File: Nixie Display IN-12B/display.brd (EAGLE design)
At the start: 161.1 x 51.6 mm, 30 parts, among them U1 TPIC6B595DWRG4, U2 TPIC6B595DWRG4, U3 TPIC6B595DWRG4, U4 TPIC6B595DWRG4, U5 TPIC6B595DWRG4, U6 TPIC6B595DWRG4, U7 TPIC6B595DWRG4, U8 TPIC6B595DWRG4, X1 22-23-2021

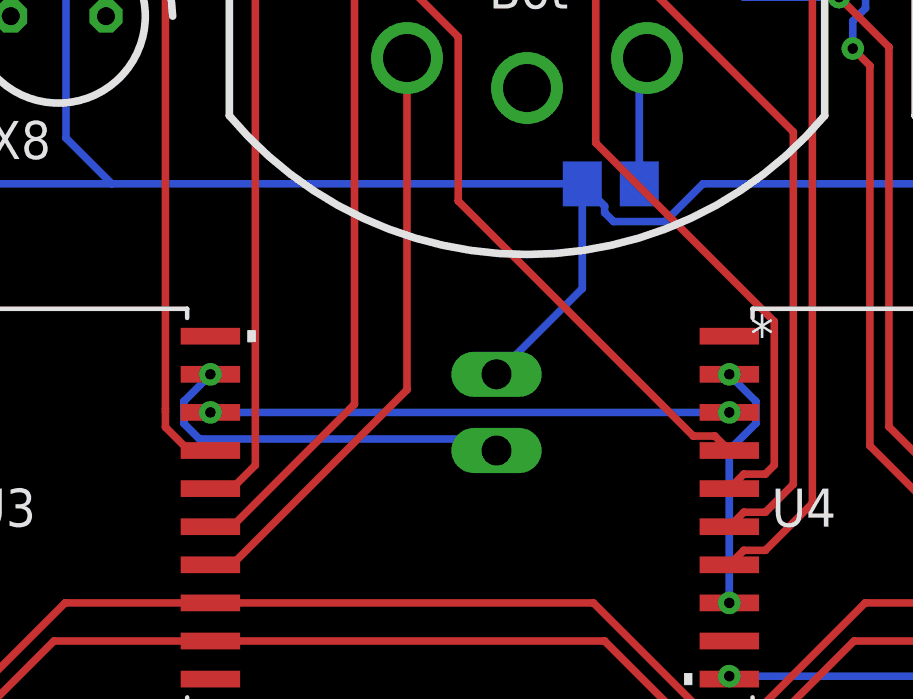
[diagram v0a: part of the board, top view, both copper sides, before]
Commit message: Begins sketch, fixes spacing and encoder circuit
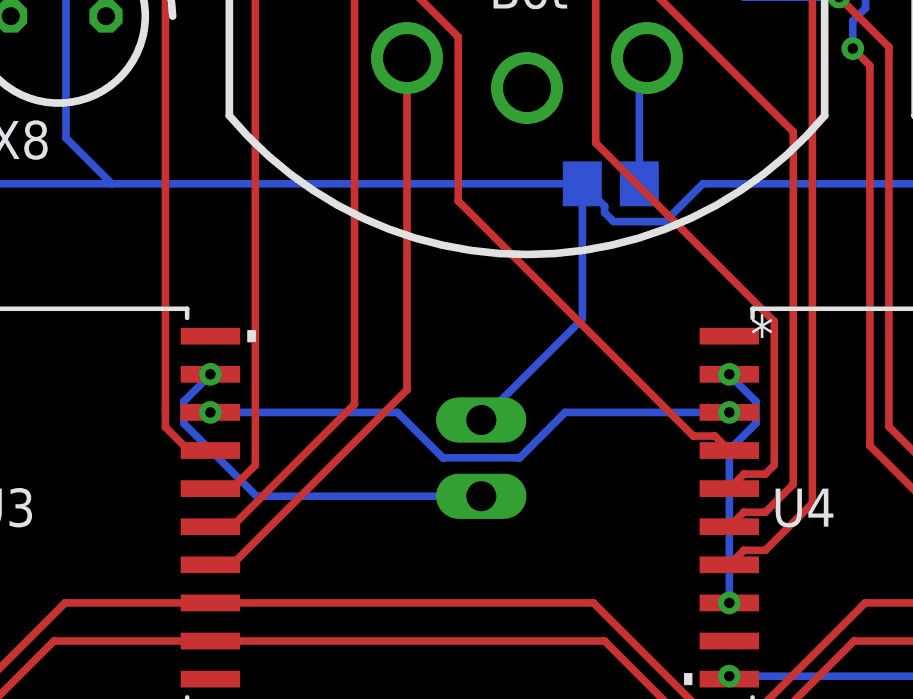
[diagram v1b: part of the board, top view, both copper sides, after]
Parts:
- moved X1 1.61 mm to (67.2, 15.1)
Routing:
- net V+: track 194.7 -> 196.5 mm
- net N$79: track 17.3 -> 18.6 mm
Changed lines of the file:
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@@
 <attribute name="VALUE" x="14.097" y="6.731" size="1.27" layer="27" ratio="10" rot="R180"/>
 </element>
-<element name="X1" library="con-molex" library_urn="urn:adsk.eagle:library:165" package="22-23-2021" package3d_urn="urn:adsk.eagle:package:8078633/1" value="22-23-2021" x="67.691" y="16.637" locked="yes" smashed="yes" rot="MR270">
-<attribute name="MF" value="MOLEX" x="67.691" y="16.637" locked="yes" size="1.778" layer="28" rot="MR270" display="off"/>
-<attribute name="MPN" value="22-23-2021" x="67.691" y="16.637" locked="yes" size="1.778" layer="28" rot="MR270" display="off"/>
-<attribute name="NAME" x="63.881" y="19.177" locked="yes" size="1.016" layer="26" ratio="10" rot="MR270"/>
-<attribute name="OC_FARNELL" value="1462926" x="67.691" y="16.637" locked="yes" size="1.778" layer="28" rot="MR270" display="off"/>
-<attribute name="OC_NEWARK" value="25C3832" x="67.691" y="16.637" locked="yes" size="1.778" layer="28" rot="MR270" display="off"/>
-<attribute name="POPULARITY" value="40" x="67.691" y="16.637" locked="yes" size="1.778" layer="28" rot="MR270" display="off"/>
-<attribute name="VALUE" x="72.771" y="19.177" locked="yes" size="1.016" layer="28" ratio="10" rot="MR270"/>
+<element name="X1" library="con-molex" library_urn="urn:adsk.eagle:library:165" package="22-23-2021" package3d_urn="urn:adsk.eagle:package:8078633/1" value="22-23-2021" x="67.183" y="15.113" smashed="yes" rot="MR270">
+<attribute name="MF" value="MOLEX" x="67.183" y="15.113" size="1.778" layer="28" rot="MR270" display="off"/>
+<attribute name="MPN" value="22-23-2021" x="67.183" y="15.113" size="1.778" layer="28" rot="MR270" display="off"/>
+<attribute name="NAME" x="63.373" y="17.653" size="1.016" layer="26" ratio="10" rot="MR270"/>
+<attribute name="OC_FARNELL" value="1462926" x="67.183" y="15.113" size="1.778" layer="28" rot="MR270" display="off"/>
+<attribute name="OC_NEWARK" value="25C3832" x="67.183" y="15.113" size="1.778" layer="28" rot="MR270" display="off"/>
+<attribute name="POPULARITY" value="40" x="67.183" y="15.113" size="1.778" layer="28" rot="MR270" display="off"/>
+<attribute name="VALUE" x="72.263" y="17.653" size="1.016" layer="28" ratio="10" rot="MR270"/>
 </element>
 <element name="NX1" library="nixies-us" package="IN-12-DSUB" value="" x="14.224" y="36.195" smashed="yes">
@@
 <via x="58.1533" y="17.907" extent="1-16" drill="0.35"/>
 <wire x1="57.2671" y1="17.00408125" x2="57.2671" y2="16.26991875" width="0.254" layer="16"/>
-<wire x1="57.2671" y1="16.26991875" x2="57.78621875" y2="15.7508" width="0.254" layer="16"/>
-<wire x1="67.3072" y1="15.7508" x2="67.691" y2="15.367" width="0.254" layer="16"/>
-<wire x1="57.78621875" y1="15.7508" x2="67.3072" y2="15.7508" width="0.254" layer="16"/>
 <wire x1="58.1533" y1="17.907" x2="58.1533" y2="17.89028125" width="0.254" layer="16"/>
 <wire x1="58.1533" y1="17.89028125" x2="57.2671" y2="17.00408125" width="0.254" layer="16"/>
@@
 <via x="147.0787" y="8.0998" extent="1-16" drill="0.35"/>
 <wire x1="147.0787" y1="8.0998" x2="147.0787" y2="8.001" width="0.254" layer="1"/>
+<wire x1="59.69401875" y1="13.843" x2="67.183" y2="13.843" width="0.254" layer="16"/>
+<wire x1="57.2671" y1="16.26991875" x2="59.69401875" y2="13.843" width="0.254" layer="16"/>
 </signal>
 <signal name="VCC">
@@
 <wire x1="51.496" y1="47.2936125" x2="52.5605" y2="46.2291125" width="0.254" layer="16"/>
 <wire x1="52.5605" y1="46.2291125" x2="52.5605" y2="42.7401" width="0.254" layer="16"/>
-<wire x1="70.551" y1="24.257" x2="70.551" y2="20.767" width="0.254" layer="16"/>
-<wire x1="70.551" y1="20.767" x2="67.691" y2="17.907" width="0.254" layer="16"/>
+<wire x1="70.551" y1="24.257" x2="70.551" y2="19.751" width="0.254" layer="16"/>
+<wire x1="70.551" y1="19.751" x2="67.183" y2="16.383" width="0.254" layer="16"/>
 <wire x1="71.293" y1="23.29658125" x2="71.59058125" y2="22.999" width="0.254" layer="16"/>
 <wire x1="71.59058125" y1="22.999" x2="73.31141875" y2="22.999" width="0.254" layer="16"/>
@@
 <contactref element="U4" pad="3"/>
 <via x="58.1533" y="16.637" extent="1-16" drill="0.35"/>
-<wire x1="58.1533" y1="16.637" x2="75.4507" y2="16.637" width="0.254" layer="16"/>
 <via x="75.4507" y="16.637" extent="1-16" drill="0.35"/>
+<wire x1="65.90625625" y1="15.121" x2="68.45974375" y2="15.121" width="0.254" layer="16"/>
+<wire x1="58.1533" y1="16.637" x2="64.39025625" y2="16.637" width="0.254" layer="16"/>
+<wire x1="69.97574375" y1="16.637" x2="75.4507" y2="16.637" width="0.254" layer="16"/>
+<wire x1="64.39025625" y1="16.637" x2="65.90625625" y2="15.121" width="0.254" layer="16"/>
+<wire x1="68.45974375" y1="15.121" x2="69.97574375" y2="16.637" width="0.254" layer="16"/>
 </signal>
 <signal name="N$27">
